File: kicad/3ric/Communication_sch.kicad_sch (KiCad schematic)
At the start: 11 parts, among them J3 PS/2 keyboard, J4 Micro_SD_Card

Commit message: update schematics
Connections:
- net GND: now also U?.9 (~{CTS})
- net ~{CTS}: no longer U?.9 (~{CTS})
- net ~{RTS}: no longer U?.8 (~{RTS})
- no-connect marks 9 -> 10
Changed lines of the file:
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@@
   (no_connect (at 74.93 50.8))
   (no_connect (at 74.93 68.58))
+  (no_connect (at 100.33 138.43))
   (no_connect (at 219.71 49.53))
   (no_connect (at 219.71 44.45))
@@
     )
   )
-  (global_label "~{CTS}" (shape input) (at 100.33 135.89 0) (fields_autoplaced)
+  (global_label "~{CS_ACIA}" (shape input) (at 100.33 151.13 0) (fields_autoplaced)
     (effects (font (size 0.9906 0.9906)) (justify left))
     (property "Intersheet References" "${INTERSHEET_REFS}" (id 0) (at -20.32 80.01 0)
@@
     )
   )
-  (global_label "~{CS_ACIA}" (shape input) (at 100.33 151.13 0) (fields_autoplaced)
-    (effects (font (size 0.9906 0.9906)) (justify left))
-    (property "Intersheet References" "${INTERSHEET_REFS}" (id 0) (at -20.32 80.01 0)
-      (effects (font (size 1.27 1.27)) hide)
-    )
-  )
   (global_label "~{CTS}" (shape input) (at 242.57 87.63 0) (fields_autoplaced)
     (effects (font (size 0.9906 0.9906)) (justify left))
@@
     (property "Intersheet References" "${INTERSHEET_REFS}" (id 0) (at 169.7652 60.8981 0)
       (effects (font (size 0.9906 0.9906)) (justify left) hide)
+    )
+  )
+  (global_label "GND" (shape input) (at 100.33 135.89 0) (fields_autoplaced)
+    (effects (font (size 0.9906 0.9906)) (justify left))
+    (property "Intersheet References" "${INTERSHEET_REFS}" (id 0) (at -20.32 59.69 0)
+      (effects (font (size 1.27 1.27)) hide)
     )
   )
@@
     )
   )
-  (global_label "~{RTS}" (shape input) (at 100.33 138.43 0) (fields_autoplaced)
-    (effects (font (size 0.9906 0.9906)) (justify left))
-    (property "Intersheet References" "${INTERSHEET_REFS}" (id 0) (at -20.32 80.01 0)
-      (effects (font (size 1.27 1.27)) hide)
-    )
-  )

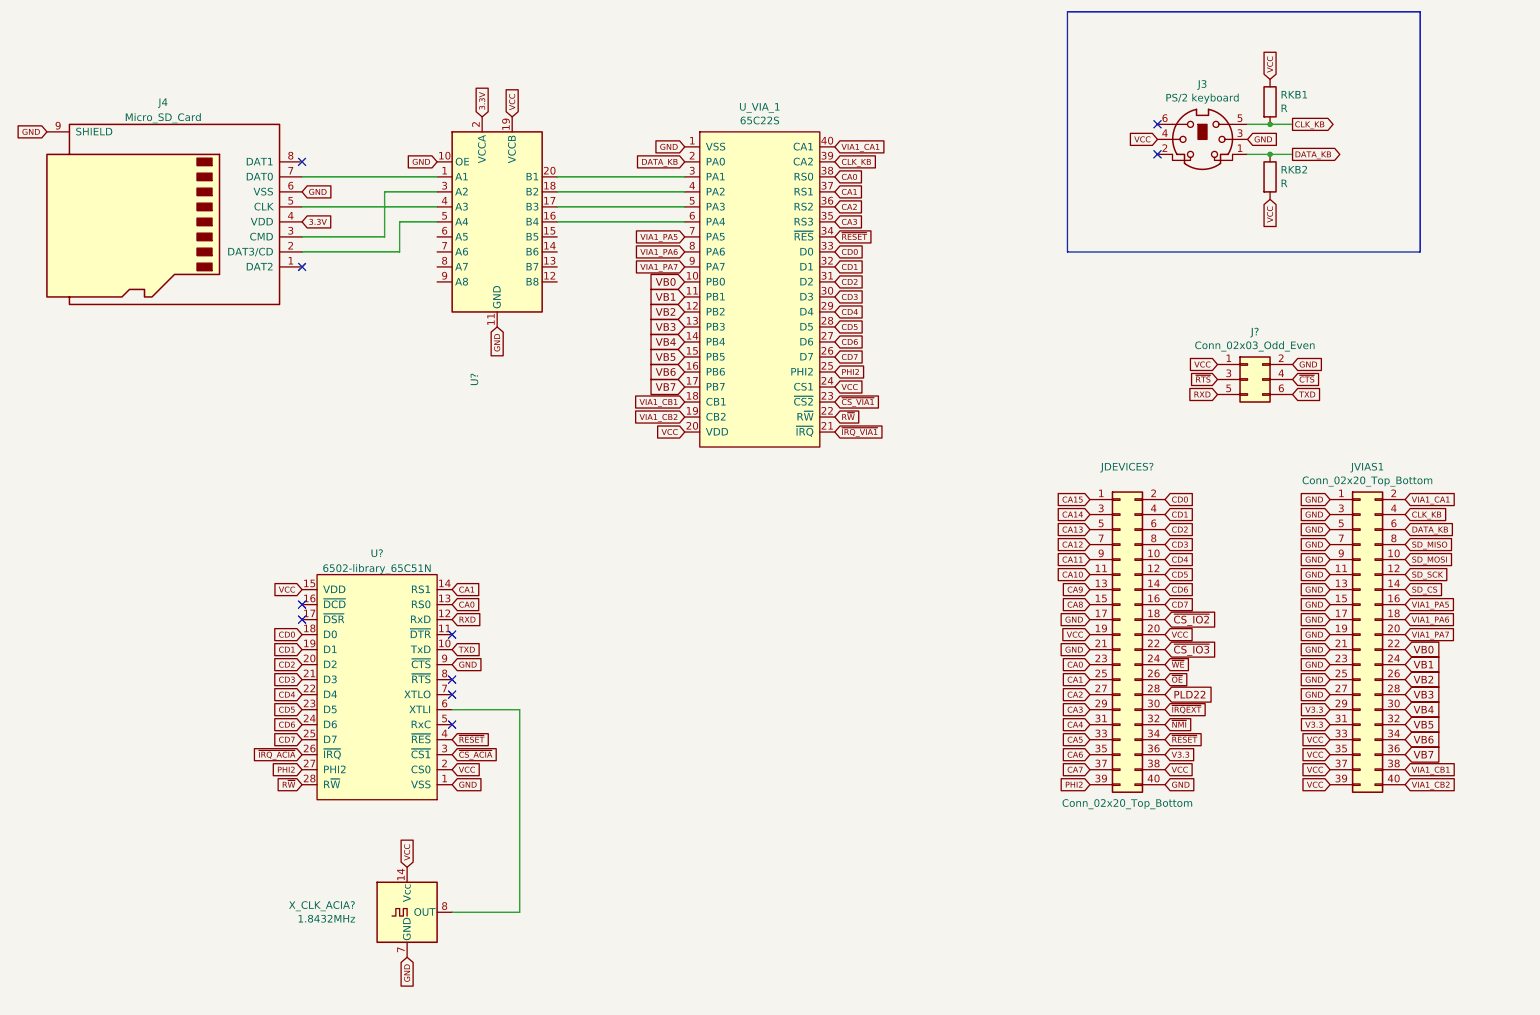
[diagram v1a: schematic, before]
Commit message: upgraded to kicad 8, updates to schematic - added snes controllers, mouse port, many fixes
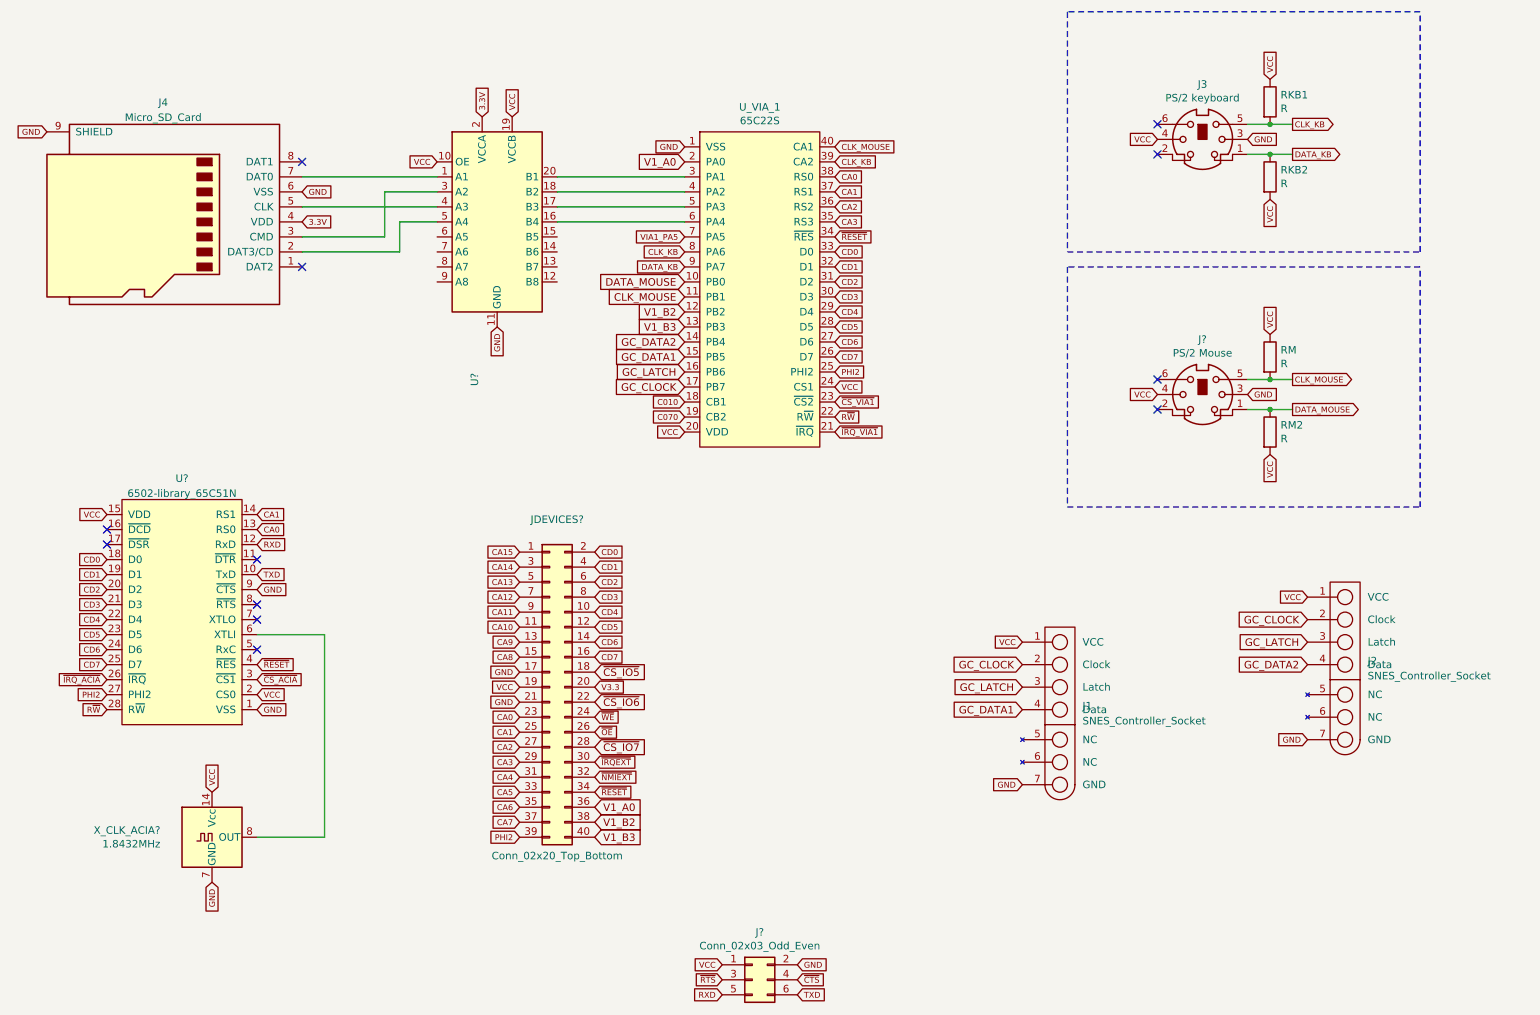
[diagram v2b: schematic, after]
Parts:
- removed JVIAS1: Conn_02x20_Top_Bottom, Connector_IDC:IDC-Header_2x20_P2.54mm_Vertical, symbol Connector_Generic:Conn_02x20_Odd_Even
- added J1, J2: SNES_Controller_Socket, Nintendo:SNES_Controller_Socket, symbol SNES-port:SNES_Controller_Socket
- added J?: PS/2 Mouse, PS2_mini_din_6:MINI-DIN-6-FULL-SHIELD, symbol Connector:Mini-DIN-6
- added RM, RM2: R, Resistor_THT:R_Axial_DIN0207_L6.3mm_D2.5mm_P7.62mm_Horizontal, symbol Device:R
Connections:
- net VIA1_CA1 is gone; now on net CLK_MOUSE: U_VIA_1.40 (CA1)
- net VIA1_PA6 is gone; now on net CLK_KB: U_VIA_1.8 (PA6)
- net VIA1_PA7 is gone; now on net DATA_KB: U_VIA_1.9 (PA7)
- net DATA_KB: no longer U_VIA_1.2 (PA0)
- net GND: now also J1.7 (GND), J2.7 (GND), J?.3; no longer JDEVICES?.40 (Pin_40), U?.10 (OE)
- net V3.3: now also JDEVICES?.20 (Pin_20); no longer JDEVICES?.36 (Pin_36)
- net VCC: now also U?.10 (OE), J1.1 (VCC), J2.1 (VCC), J?.4, RM.1, RM2.2; no longer JDEVICES?.20 (Pin_20), JDEVICES?.38 (Pin_38)
- net PLD22 renamed ~{CS_IO7}
- net VB0 renamed DATA_MOUSE
- net DATA_MOUSE: now also J?.1, RM2.1
- net VB1 renamed CLK_MOUSE
- net CLK_MOUSE: now also J?.5, RM.2
- net VB2 renamed V1_B2
- net V1_B2: now also JDEVICES?.38 (Pin_38)
- net VB3 renamed V1_B3
- net V1_B3: now also JDEVICES?.40 (Pin_40)
- net VB4 renamed GC_DATA2
- net GC_DATA2: now also J2.4 (Data)
- net VB5 renamed GC_DATA1
- net GC_DATA1: now also J1.4 (Data)
- net VB6 renamed GC_LATCH
- net GC_LATCH: now also J1.3 (Latch), J2.3 (Latch)
- net VB7 renamed GC_CLOCK
- net GC_CLOCK: now also J1.2 (Clock), J2.2 (Clock)
- net VIA1_CB1 renamed C010
- net VIA1_CB2 renamed C070
- net ~{CS_IO2} renamed ~{CS_IO5}
- net ~{CS_IO3} renamed ~{CS_IO6}
- net ~{NMI} renamed ~{NMIEXT}
- new net V1_A0: JDEVICES?.36 (Pin_36), U_VIA_1.2 (PA0)
- no-connect marks 10 -> 12
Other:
- moved on the sheet: J?, JDEVICES?, U?, X_CLK_ACIA?
